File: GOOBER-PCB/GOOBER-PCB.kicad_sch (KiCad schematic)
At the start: 0 parts

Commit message: worked on adding 12v to 5v
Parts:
- added C1, C2, C7: 10uF, Capacitor_SMD:C_0805_2012Metric_Pad1.18x1.45mm_HandSolder, symbol Device:C
- added C3, C4, C8: 0.1uF, Capacitor_SMD:C_0805_2012Metric_Pad1.18x1.45mm_HandSolder, symbol Device:C
- added C5, C6: 22uF, Capacitor_SMD:C_0805_2012Metric_Pad1.18x1.45mm_HandSolder, symbol Device:C
- added D1, D2, D3: LED, Diode_SMD:D_0805_2012Metric_Pad1.15x1.40mm_HandSolder, symbol Device:LED
- added J1, J6: XT30U_F, Connector_AMASS:AMASS_XT30PW-M_1x02_P2.50mm_Horizontal, symbol Connector_Generic:Conn_01x02
- added J2, J3: Conn_01x22, symbol Connector_Generic:Conn_01x22
- added L1: 3.3uH, Inductor_SMD:L_TDK_VLS6045EX_VLS6045AF, symbol Device:L_Ferrite
- added Q2: PJD15P06A_L2_00001, Package_TO_SOT_SMD:TO-252-2, symbol Device:Q_PMOS
- added R1: 54.9K, Resistor_SMD:R_0805_2012Metric_Pad1.20x1.40mm_HandSolder, symbol Device:R_US
- added R11, R2: 10K, Resistor_SMD:R_0805_2012Metric_Pad1.20x1.40mm_HandSolder, symbol Device:R_US
- added R13: 0, Resistor_SMD:R_1210_3225Metric_Pad1.30x2.65mm_HandSolder, symbol Device:R_US
- added R3, R4, R5: 1K, Resistor_SMD:R_0805_2012Metric_Pad1.20x1.40mm_HandSolder, symbol Device:R_US
- added R9: 100, Resistor_SMD:R_0805_2012Metric_Pad1.20x1.40mm_HandSolder, symbol Device:R_US
- added U1: TPS565208, Package_TO_SOT_SMD:SOT-23-6, symbol Regulator_Switching:TPS565208
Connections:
- new net: C1.1, C2.1, C3.1, Q2.S, R13.1, U1.3 (VIN)
- new net: Q2.G, R9.1
- new net: R11.1, U1.5 (EN)
- new net: D2.2 (A), R3.2
- new net: D3.2 (A), R5.2
- new net: C4.2, L1.1, U1.2 (SW)
- new net: D1.2 (A), R4.2
- new net: R1.1, R2.2, U1.4 (VFB)
- new net: C4.1, U1.6 (VBST)
- new net +12V: D3.1 (K), J1.1 (Pin_1), J6.1 (Pin_1), Q2.D, R11.2, R13.2, R3.1
- new net +5V: C5.1, C6.1, C7.1, C8.1, J2.21 (Pin_21), L1.2, R1.2, R4.1
- new net GND: C1.2, C2.2, C3.2, C5.2, C6.2, C7.2, C8.2, D1.1 (K), D2.1 (K), J1.2 (Pin_2), J2.22 (Pin_22), J3.1 (Pin_1), J3.21 (Pin_21), J3.22 (Pin_22), J6.2 (Pin_2), R2.1, R5.1, R9.2, U1.1 (GND)
- new net MTDI: J3.7 (Pin_7), J3.8 (Pin_8)
- no-connect marks 0 -> 3
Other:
- note added: "12V IN Battery and Charger"
- note added: "12V to 5V, 3A"
- note added: "ESP32"
- note added: "POWER"

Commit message: did a lot of work for schematic
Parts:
- added C10, C12: 0.1uF, Capacitor_SMD:C_0805_2012Metric_Pad1.18x1.45mm_HandSolder, symbol Device:C
- added C11, C9: 10uF, Capacitor_SMD:C_0805_2012Metric_Pad1.18x1.45mm_HandSolder, symbol Device:C
- added D5: CDBW140-G, Diode_SMD:D_SOD-123, symbol Device:D_Schottky
- added F6: 1A, Fuse:Fuseholder_Blade_Mini_Keystone_3568, symbol Device:Fuse
- added J4, J5: Conn_01x22, Connector_PinHeader_2.54mm:PinHeader_1x22_P2.54mm_Vertical, symbol Connector_Generic:Conn_01x22
- added J7: USB_C_Receptacle_USB2.0_14P, Connector_USB:USB_C_Receptacle_GCT_USB4115-03-C, symbol Connector:USB_C_Receptacle_USB2.0_14P
- added Q3: AO3419, Package_TO_SOT_SMD:SOT-23, symbol Device:Q_PMOS
- added R6: 100K, Resistor_SMD:R_0805_2012Metric_Pad1.20x1.40mm_HandSolder, symbol Device:R_US
- added R7, R8: 5.1K, Resistor_SMD:R_0805_2012Metric_Pad1.20x1.40mm_HandSolder, symbol Device:R_US
- added TP1, TP10, TP11, TP12, TP13, TP14, TP15, TP16, TP17, TP18, TP19, TP2, TP20, TP21, TP22, TP23, TP24, TP25, TP26, TP27, TP28, TP29, TP3, TP30, TP31, TP32, TP33, TP34, TP35, TP36, TP37, TP38, TP39, TP4, TP40, TP41, TP42, TP43, TP5, TP6, TP7, TP8, TP9: TP, TestPoint:TestPoint_Keystone_5000-5004_Miniature, symbol Connector:TestPoint_Probe
- D1, D2, D3: footprint Diode_SMD:D_0805_2012Metric_Pad1.15x1.40mm_HandSolder -> LED_SMD:LED_0805_2012Metric
- J2, J3: footprint (none) -> Connector_PinHeader_2.54mm:PinHeader_1x22_P2.54mm_Vertical
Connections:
- net +12V: now also F6.2, TP40.1; no longer Q2.D, R13.2
- net +5V: now also J4.1 (Pin_1), J4.2 (Pin_2), Q3.D, TP39.1; no longer C7.1, C8.1, J2.21 (Pin_21)
- net GND: now also C10.2, C11.2, C12.2, C9.2, J4.22 (Pin_22), J5.1 (Pin_1), J5.21 (Pin_21), J5.22 (Pin_22), J7.A1 (GND), J7.A12 (GND), J7.B1 (GND), J7.B12 (GND), J7.S1 (SHIELD), R6.1, R7.2, R8.2, TP41.1, TP42.1, TP43.1
- net MTDI: now also J5.7 (Pin_7), TP24.1; no longer J3.8 (Pin_8)
- net GPIO17: now reaches J2.10 (Pin_10)
- net GPIO17: now also J4.10 (Pin_10), TP8.1
- net GPIO18: now reaches J2.11 (Pin_11)
- net GPIO18: now also J4.11 (Pin_11), TP9.1
- net GPIO8: now reaches J2.12 (Pin_12)
- net GPIO8: now also J4.12 (Pin_12), TP10.1
- net GPIO3: now reaches J2.13 (Pin_13)
- net GPIO3: now also J4.13 (Pin_13), TP11.1
- net GPIO46: now reaches J2.14 (Pin_14)
- net GPIO46: now also J4.14 (Pin_14), TP12.1
- net GPIO9: now reaches J2.15 (Pin_15)
- net GPIO9: now also J4.15 (Pin_15), TP13.1
- net GPIO10: now reaches J2.16 (Pin_16)
- net GPIO10: now also J4.16 (Pin_16), TP14.1
- net GPIO11: now reaches J2.17 (Pin_17)
- net GPIO11: now also J4.17 (Pin_17), TP15.1
- net GPIO12: now reaches J2.18 (Pin_18)
- net GPIO12: now also J4.18 (Pin_18), TP16.1
- net GPIO13: now reaches J2.19 (Pin_19)
- net GPIO13: now also J4.19 (Pin_19), TP17.1
- net GPIO14: now reaches J2.20 (Pin_20)
- net GPIO14: now also J4.20 (Pin_20), TP18.1
- net RST: now reaches J2.3 (Pin_3)
- net RST: now also J4.3 (Pin_3), TP1.1
- net GPIO4: now reaches J2.4 (Pin_4)
- net GPIO4: now also J4.4 (Pin_4), TP2.1
- net GPIO5: now reaches J2.5 (Pin_5)
- net GPIO5: now also J4.5 (Pin_5), TP3.1
- net GPIO6: now reaches J2.6 (Pin_6)
- net GPIO6: now also J4.6 (Pin_6), TP4.1
- net GPIO7: now reaches J2.7 (Pin_7)
- net GPIO7: now also J4.7 (Pin_7), TP5.1
- net GPIO15: now reaches J2.8 (Pin_8)
- net GPIO15: now also J4.8 (Pin_8), TP6.1
- net GPIO16: now reaches J2.9 (Pin_9)
- net GPIO16: now also J4.9 (Pin_9), TP7.1
- net GPIO38: now reaches J3.10 (Pin_10)
- net GPIO38: now also J5.10 (Pin_10), TP27.1
- net GPIO37: now reaches J3.11 (Pin_11)
- net GPIO37: now also J5.11 (Pin_11), TP28.1
- net GPIO36: now reaches J3.12 (Pin_12)
- net GPIO36: now also J5.12 (Pin_12), TP29.1
- net GPIO35: now reaches J3.13 (Pin_13)
- net GPIO35: now also J5.13 (Pin_13), TP30.1
- net GPIO0: now reaches J3.14 (Pin_14)
- net GPIO0: now also J5.14 (Pin_14), TP31.1
- net GPIO45: now reaches J3.15 (Pin_15)
- net GPIO45: now also J5.15 (Pin_15), TP32.1
- net SPICLK_P: now reaches J3.16 (Pin_16)
- net SPICLK_P: now also J5.16 (Pin_16), TP33.1
- net SPICLK_N: now reaches J3.17 (Pin_17)
- net SPICLK_N: now also J5.17 (Pin_17), TP34.1
- net RTC: now reaches J3.18 (Pin_18)
- net RTC: now also J5.18 (Pin_18), TP35.1
- net USBD_P: now reaches J3.19 (Pin_19)
- net USBD_P: now also J5.19 (Pin_19), J7.A6 (D+), J7.B6 (D+), TP36.1
- net U0_TX: now reaches J3.2 (Pin_2)
- net U0_TX: now also J5.2 (Pin_2), TP19.1
- net USBD_N: now reaches J3.20 (Pin_20)
- net USBD_N: now also J5.20 (Pin_20), J7.A7 (D-), J7.B7 (D-), TP37.1
- net U0_RX: now reaches J3.3 (Pin_3)
- net U0_RX: now also J5.3 (Pin_3), TP20.1
- net GPIO1: now reaches J3.4 (Pin_4)
- net GPIO1: now also J5.4 (Pin_4), TP21.1
- net GPIO2: now reaches J3.5 (Pin_5)
- net GPIO2: now also J5.5 (Pin_5), TP22.1
- net MTMS: now reaches J3.6 (Pin_6)
- net MTMS: now also J5.6 (Pin_6), TP23.1
- net MTCK: now reaches J3.9 (Pin_9)
- net MTCK: now also J5.9 (Pin_9), TP26.1
- new net: F6.1, Q2.D, R13.2
- new net: J7.A5 (CC1), R7.1
- new net: J7.B5 (CC2), R8.1
- new net +5VA: C10.1, C11.1, C12.1, C7.1, C8.1, C9.1, D5.1 (K), J2.21 (Pin_21), J4.21 (Pin_21), Q3.S
- new net MTDO: J3.8 (Pin_8), J5.8 (Pin_8), TP25.1
- new net VBUS: D5.2 (A), J7.A4 (VBUS), J7.A9 (VBUS), J7.B4 (VBUS), J7.B9 (VBUS), Q3.G, R6.2, TP38.1
- no-connect marks 3 -> 2
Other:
- note added: "5V CHOOSER"
- note added: "Breakout Headers"
- note added: "Test Points"
- note added: "USB C IN"
- note removed: "POWER"
- moved on the sheet: C1, C2, C3, C4, C5, C6, C7, C8, D1, D2, D3, J1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

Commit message: did some layout
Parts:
- removed J7: USB_C_Receptacle_USB2.0_14P, Connector_USB:USB_C_Receptacle_GCT_USB4115-03-C, symbol Connector:USB_C_Receptacle_USB2.0_14P
- removed Q2: PJD15P06A_L2_00001, Package_TO_SOT_SMD:TO-252-2, symbol Device:Q_PMOS
- removed Q3: AO3419, Package_TO_SOT_SMD:SOT-23, symbol Device:Q_PMOS
- added F7: 1A, Fuse:Fuseholder_Blade_Mini_Keystone_3568, symbol Device:Fuse
- added H1, H2, H3: MountingHole, MountingHole:MountingHole_3.2mm_M3_ISO7380, symbol Mechanical:MountingHole
- added J8: USB C vertical, Connector_USB:USB_C_Receptacle_GCT_USB4115-03-C, symbol Connector:USB_C_Receptacle_USB2.0_14P
- added Q3: PJD15P06A_L2_00001, Package_TO_SOT_SMD:TO-252-2, symbol Transistor_FET:Q_PMOS_GDS
- added Q4: AO3419, Package_TO_SOT_SMD:SOT-23_Handsoldering, symbol Transistor_FET:Q_PMOS_GDS
- added TP44, TP46: TP, TestPoint:TestPoint_Keystone_5000-5004_Miniature, symbol Connector:TestPoint_Probe
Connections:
- net +12V: now also J1.2 (Pin_2), J6.2 (Pin_2); no longer J1.1 (Pin_1), J6.1 (Pin_1)
- net +5V: now also F7.1, Q4.2 (D); no longer C5.1, C6.1, J4.1 (Pin_1), J4.2 (Pin_2), L1.2, R1.2
- net +5VA: now also J4.1 (Pin_1), J4.2 (Pin_2), Q4.3 (S), TP44.1
- net GND: now also J1.1 (Pin_1), J6.1 (Pin_1), J8.A1 (GND), J8.A12 (GND), J8.B1 (GND), J8.B12 (GND), J8.SH (SHIELD), TP46.1; no longer J1.2 (Pin_2), J6.2 (Pin_2)
- net USBD_N: now also J8.A7 (D-), J8.B7 (D-)
- net USBD_P: now also J8.A6 (D+), J8.B6 (D+)
- net VBUS: now also J8.A4 (VBUS), J8.A9 (VBUS), J8.B4 (VBUS), J8.B9 (VBUS), Q4.1 (G)
- net at C1.1, C2.1, C3.1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: now also Q3.3 (S)
- net at F6.1, R13.2: now also Q3.2 (D)
- net at R9.1: now also Q3.1 (G)
- net at R7.1: now also J8.A5 (CC1)
- net at R8.1: now also J8.B5 (CC2)
- new net: C5.1, C6.1, F7.2, L1.2, R1.2
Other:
- note added: "Mounting Holes"
- moved on the sheet: D1, R4

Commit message: some work on pcb
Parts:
- added C13: 0.1uF, Capacitor_SMD:C_0805_2012Metric_Pad1.18x1.45mm_HandSolder, symbol Device:C
- added J20: BM04B-SRSS-TB, Connector_JST:JST_SH_BM04B-SRSS-TB_1x04-1MP_P1.00mm_Vertical, symbol QWIIC:PRT-14417
- added J7, J9: Conn_01x08, Connector_PinHeader_2.54mm:PinHeader_1x08_P2.54mm_Vertical, symbol Connector_Generic:Conn_01x08
- added R12, R15, R19: 10K, Resistor_SMD:R_0805_2012Metric_Pad1.20x1.40mm_HandSolder, symbol Device:R_US
- added TP45: TP, TestPoint:TestPoint_Keystone_5000-5004_Miniature, symbol Connector:TestPoint_Probe
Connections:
- net +5VA: no longer J4.2 (Pin_2)
- net GND: now also C13.2, J20.4, J7.2 (Pin_2), J7.7 (Pin_7), J9.2 (Pin_2)
- net GPIO10: now also J9.8 (Pin_8)
- net GPIO11: now also J9.7 (Pin_7)
- net GPIO12: now also J7.3 (Pin_3)
- net GPIO13: now also J7.4 (Pin_4)
- net GPIO14: now also J7.5 (Pin_5)
- net GPIO8: now also J20.1, R19.1
- net GPIO9: now also J20.2, R15.1
- net +3V3: now reaches J2.1 (Pin_1)
- net +3V3: now also J2.2 (Pin_2), J4.2 (Pin_2), C13.1, J20.3, J7.8 (Pin_8), R12.1, R15.2, R19.2, TP45.1
- net MTCK renamed CLK
- net CLK: now also J9.4 (Pin_4)
- net MTDI renamed MOSI
- net MOSI: now also J9.5 (Pin_5)
- net MTDO renamed MISO
- net MISO: now also J9.6 (Pin_6)
- net MTMS renamed CS
- net CS: now also J9.3 (Pin_3), R12.2
- no-connect marks 2 -> 3
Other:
- note added: "QWIIC"
- note added: "Radio Module"

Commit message: first revision of goober pcb
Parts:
- removed TP36, TP37: TP, TestPoint:TestPoint_Keystone_5000-5004_Miniature, symbol Connector:TestPoint_Probe
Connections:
- net GPIO0: now also J9.8 (Pin_8)
- net GPIO10: no longer J9.8 (Pin_8)
- net GPIO11: no longer J9.7 (Pin_7)
- net GPIO12: no longer J7.3 (Pin_3)
- net GPIO13: no longer J7.4 (Pin_4)
- net GPIO14: no longer J7.5 (Pin_5)
- net GPIO35: now also J9.7 (Pin_7)
- net GPIO36: now also J7.5 (Pin_5)
- net GPIO37: now also J7.4 (Pin_4)
- net GPIO38: now also J7.3 (Pin_3)

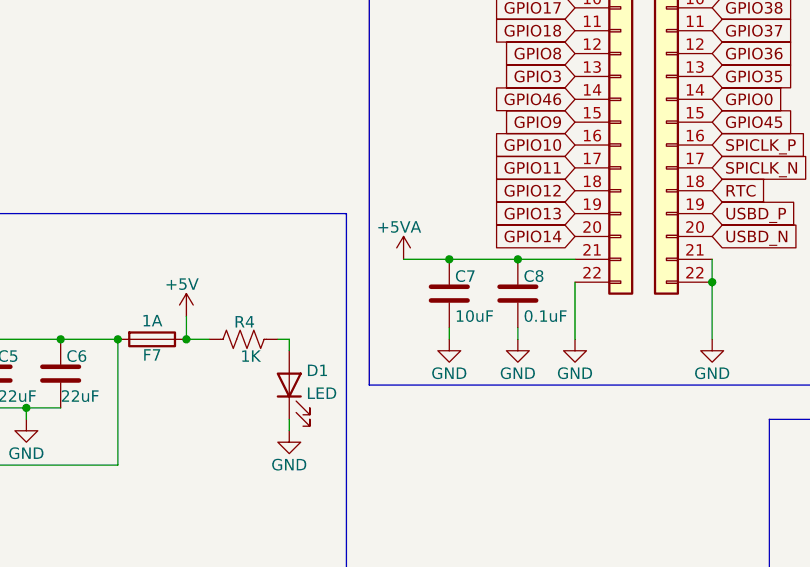
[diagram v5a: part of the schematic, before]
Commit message: added 47uF cap
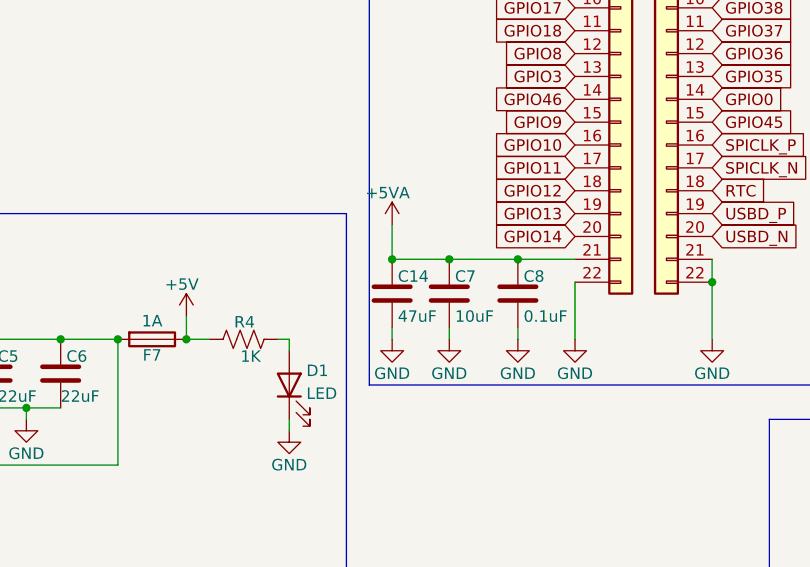
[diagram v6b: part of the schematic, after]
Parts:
- added C14: 47uF, Capacitor_SMD:C_1206_3216Metric_Pad1.33x1.80mm_HandSolder, symbol Device:C
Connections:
- net +5VA: now also C14.1
- net GND: now also C14.2
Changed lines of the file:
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@@
 	)
 	(junction
+		(at 179.07 73.66)
+		(diameter 0)
+		(color 0 0 0 0)
+	)
+	(junction
 		(at 77.47 130.81)
 		(diameter 0)
@@
 	)
 	(junction
-		(at 60.96 85.09)
+		(at 172.72 73.66)
 		(diameter 0)
 		(color 0 0 0 0)
 	)
 	(junction
-		(at 45.72 139.7)
+		(at 60.96 85.09)
 		(diameter 0)
 		(color 0 0 0 0)
 	)
 	(junction
-		(at 92.71 137.16)
+		(at 45.72 139.7)
 		(diameter 0)
 		(color 0 0 0 0)
 	)
 	(junction
-		(at 179.07 73.66)
+		(at 92.71 137.16)
 		(diameter 0)
 		(color 0 0 0 0)
@@
 	(wire
 		(pts
+			(xy 172.72 81.28) (xy 172.72 82.55)
+		)
+		(stroke
+			(width 0)
+			(type default)
+		)
+	)
+	(wire
+		(pts
 			(xy 193.04 22.86) (xy 193.04 25.4)
 		)
@@
 	(wire
 		(pts
+			(xy 172.72 69.85) (xy 172.72 73.66)
+		)
+		(stroke
+			(width 0)
+			(type default)
+		)
+	)
+	(wire
+		(pts
 			(xy 265.43 73.66) (xy 265.43 76.2)
 		)
@@
 	(wire
 		(pts
-			(xy 173.99 73.66) (xy 179.07 73.66)
-		)
-		(stroke
-			(width 0)
-			(type default)
-		)
-	)
-	(wire
-		(pts
 			(xy 36.83 102.87) (xy 36.83 101.6)
 		)
@@
 	(wire
 		(pts
+			(xy 172.72 73.66) (xy 179.07 73.66)
+		)
+		(stroke
+			(width 0)
+			(type default)
+		)
+	)
+	(wire
+		(pts
 			(xy 251.46 144.78) (xy 233.68 144.78)
 		)
@@
 	)
 	(symbol
+		(lib_id "Device:C")
+		(at 172.72 77.47 0)
+		(unit 1)
+		(body_style 1)
+		(exclude_from_sim no)
+		(in_bom yes)
+		(on_board yes)
+		(in_pos_files yes)
+		(dnp no)
+		(property "Reference" "C14"
+			(at 173.355 75.5649 0)
+			(show_name no)
+			(do_not_autoplace no)
+			(effects
+				(font
+					(size 1.27 1.27)
+				)
+				(justify left)
+			)
+		)
+		(property "Value" "47uF"
+			(at 173.355 80.0099 0)
+			(show_name no)
+			(do_not_autoplace no)
+			(effects
+				(font
+					(size 1.27 1.27)
+				)
+				(justify left)
+			)
+		)
+		(property "Footprint" "Capacitor_SMD:C_1206_3216Metric_Pad1.33x1.80mm_HandSolder"
+			(at 173.6852 81.28 0)
+			(hide yes)
+			(show_name no)
+			(do_not_autoplace no)
+			(effects
+				(font
+					(size 1.27 1.27)
+				)
+			)
+		)
+		(property "Datasheet" "https://www.digikey.com/en/products/detail/murata-electronics/GRM31CR61A476ME15L/2334879"
+			(at 172.72 77.47 0)
+			(hide yes)
+			(show_name no)
+			(do_not_autoplace no)
+			(effects
+				(font
+					(size 1.27 1.27)
+				)
+			)
+		)
+		(property "Description" "Unpolarized capacitor"
+			(at 172.72 77.47 0)
+			(hide yes)
+			(show_name no)
+			(do_not_autoplace no)
+			(effects
+				(font
+					(size 1.27 1.27)
+				)
+			)
+		)
+		(pin "1"
+		)
+		(pin "2"
+		)
+		(instances
+			(project "GOOBER-PCB"
+				(path "/69d2e9b3-bdf1-40d9-9a29-fed7046e6c20"
+					(reference "C14")
+					(unit 1)
+				)
+			)
+		)
+	)
+	(symbol
 		(lib_id "Device:R_US")
 		(at 80.01 95.25 270)
@@
 	)
 	(symbol
+		(lib_id "power:GND")
+		(at 172.72 82.55 0)
+		(unit 1)
+		(body_style 1)
+		(exclude_from_sim no)
+		(in_bom yes)
+		(on_board yes)
+		(in_pos_files yes)
+		(dnp no)
+		(property "Reference" "#PWR054"
+			(at 172.72 88.9 0)
+			(hide yes)
+			(show_name no)
+			(do_not_autoplace no)
+			(effects
+				(font
+					(size 1.27 1.27)
+				)
+			)
+		)
+		(property "Value" "GND"
+			(at 172.72 86.36 0)
+			(show_name no)
+			(do_not_autoplace no)
+			(effects
+				(font
+					(size 1.27 1.27)
+				)
+			)
+		)
+		(property "Footprint" ""
+			(at 172.72 82.55 0)
+			(hide yes)
+			(show_name no)
+			(do_not_autoplace no)
+			(effects
+				(font
+					(size 1.27 1.27)
+				)
+			)
+		)
+		(property "Datasheet" ""
+			(at 172.72 82.55 0)
+			(hide yes)
+			(show_name no)
+			(do_not_autoplace no)
+			(effects
+				(font
+					(size 1.27 1.27)
+				)
+			)
+		)
+		(property "Description" "Power symbol creates a global label with name \"GND\" , ground"
+			(at 172.72 82.55 0)
+			(hide yes)
+			(show_name no)
+			(do_not_autoplace no)
+			(effects
+				(font
+					(size 1.27 1.27)
+				)
+			)
+		)
+		(pin "1"
+		)
+		(instances
+			(project "GOOBER-PCB"
+				(path "/69d2e9b3-bdf1-40d9-9a29-fed7046e6c20"
+					(reference "#PWR054")
+					(unit 1)
+				)
+			)
+		)
+	)
+	(symbol
 		(lib_id "Device:C")
 		(at 179.07 77.47 0)
@@
 	(symbol
 		(lib_id "power:+5VA")
-		(at 173.99 73.66 0)
+		(at 172.72 69.85 0)
 		(unit 1)
 		(body_style 1)
@@
 		(dnp no)
 		(property "Reference" "#PWR05"
-			(at 173.99 77.47 0)
+			(at 172.72 73.66 0)
 			(hide yes)
 			(show_name no)
@@
 		)
 		(property "Value" "+5VA"
-			(at 173.482 70.104 0)
+			(at 172.212 66.294 0)
 			(show_name no)
 			(do_not_autoplace no)
@@
 		)
 		(property "Footprint" ""
-			(at 173.99 73.66 0)
+			(at 172.72 69.85 0)
 			(hide yes)
 			(show_name no)
@@
 		)
 		(property "Datasheet" ""
-			(at 173.99 73.66 0)
+			(at 172.72 69.85 0)
 			(hide yes)
 			(show_name no)
@@
 		)
 		(property "Description" "Power symbol creates a global label with name \"+5VA\""
-			(at 173.99 73.66 0)
+			(at 172.72 69.85 0)
 			(hide yes)
 			(show_name no)
